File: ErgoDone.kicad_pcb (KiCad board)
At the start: 2 copper layers, 182.8 x 158.9 mm, 152 parts, among them J1 USB, J2 3.5mm, J3 JMP, J4 JMP, SW0:10 SW0:3, SW0:11 SW0:2, SW0:12 SW0:1, SW0:7 SW0:6, SW0:8 SW0:5, SW0:9 SW0:4, SW1:10 SW1:3, SW1:11 SW1:2, SW1:12 SW1:1, SW1:13 SW1:0, SW1:9 SW1:4, SW2:10 SW2:3, SW2:11 SW2:2, SW2:12 SW2:1, SW2:13 SW2:0, SW2:7 SW2:6, SW2:8 SW2:5, SW2:9 SW2:4, SW3:10 SW3:3, SW3:11 SW3:2, SW3:12 SW3:1, SW3:13 SW3:0, SW3:7 SW3:6, SW3:8 SW3:5, SW3:9 SW3:4, SW4:10 SW4:3, SW4:11 SW4:2, SW4:12 SW4:1, SW4:13 SW4:0, SW4:7 SW4:6, SW4:8 SW4:5, SW4:9 SW4:4, SW5:10 SW5:3, SW5:11 SW5:2, SW5:12 SW5:1, SW5:13 SW5:0, SW5:7 SW5:6, SW5:8 SW5:5, SW5:9 SW5:4, U1 ProMicro, U2 MCP23017

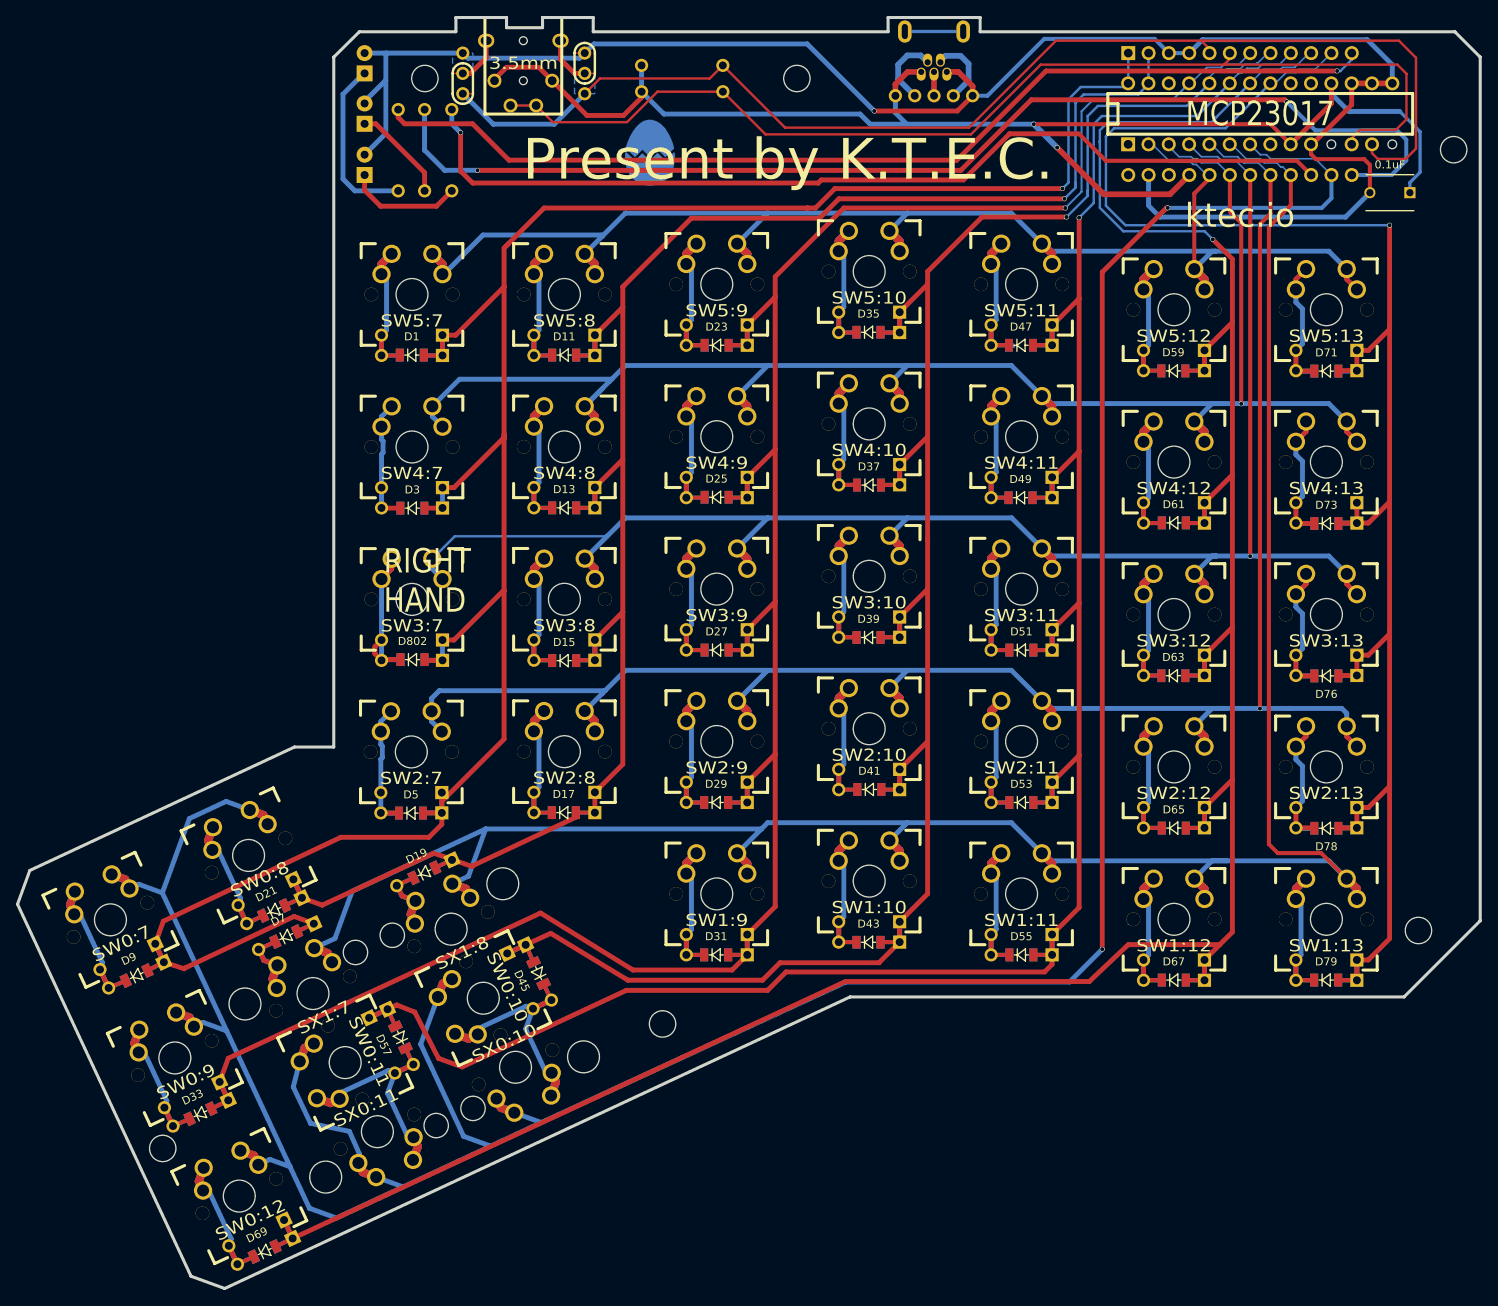
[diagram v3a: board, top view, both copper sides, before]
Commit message: Change in PCB size and silkscreen changes.
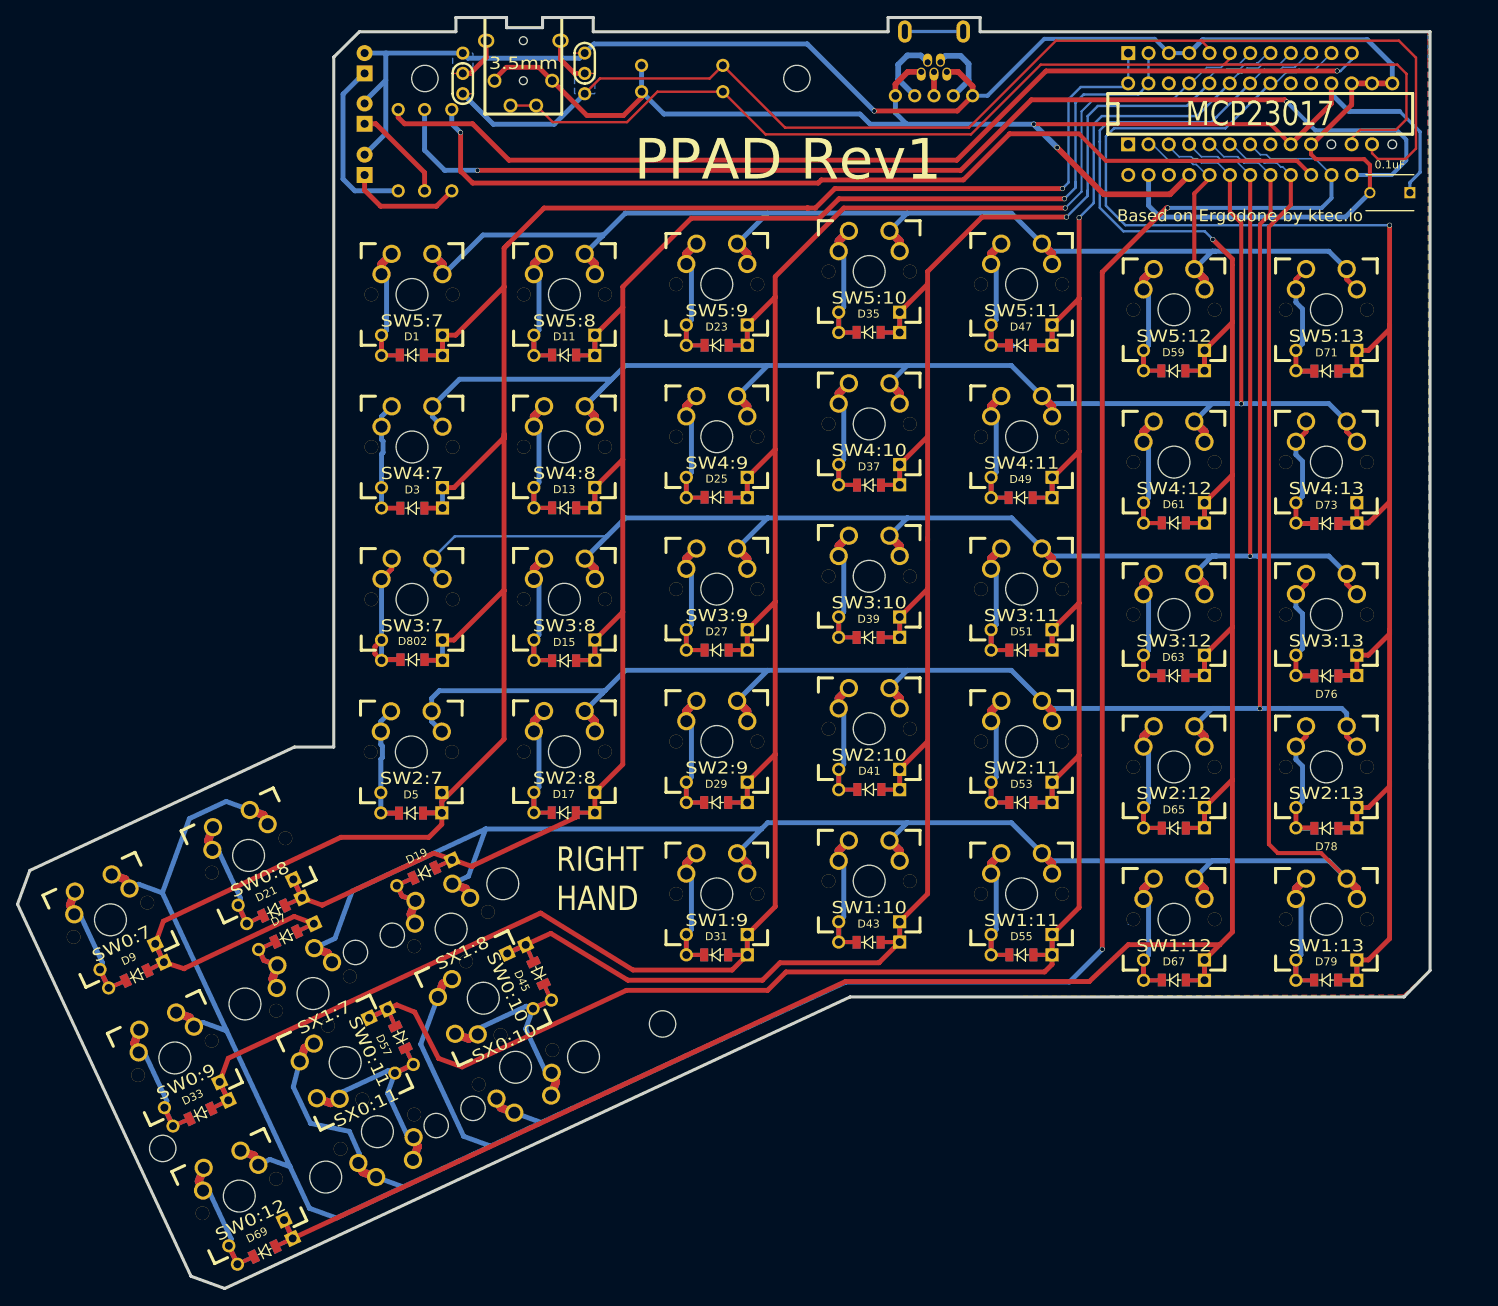
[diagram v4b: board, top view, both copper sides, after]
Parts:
- removed the G*** at (102.2, 48.4)
- removed the REF** at (198.2, 144.6)
- removed the REF** at (202.6, 47.0)
- added ?: , , F.Cu at (102.1, 47.0)
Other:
- board size 182.8 x 158.9 mm -> 176.6 x 158.9 mm
- board text added: "Based on Ergodone by ktec.io"
- board text added: "PPAD Rev1"
- board text removed: "ErgoD ne"
- board text removed: "Present by K.T.E.C."
- board text removed: "Special Thanks to riginal ErgoDOX Designers"
- board text removed: "ktec.io"
